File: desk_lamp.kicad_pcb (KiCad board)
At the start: 2 copper layers, 55 x 37 mm, 31 parts, among them J1 CON-SOCJ-2155, J2 CON-SOCJ-2155, J3 Phoenix_Contact_1989764, Q1 2N7002K, Q2 MCB150N06YB-TP, U1 MCP1799T-3302H_DB, U2 MIC5365-1.2YC5-TR, U3 ECS-TXO-25CSMV-320-AM-TR, U4 ICE40LP384-SG32, U5 W25X10CLSNIG

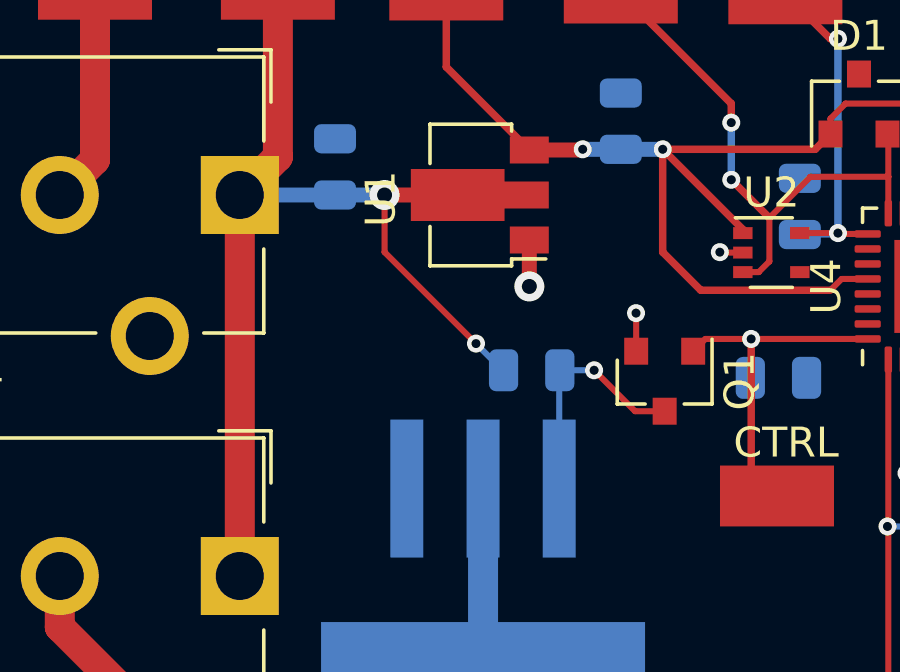
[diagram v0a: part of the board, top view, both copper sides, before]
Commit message: Fixed mosfet swapped pins
Gate and Drain pins were swapped.
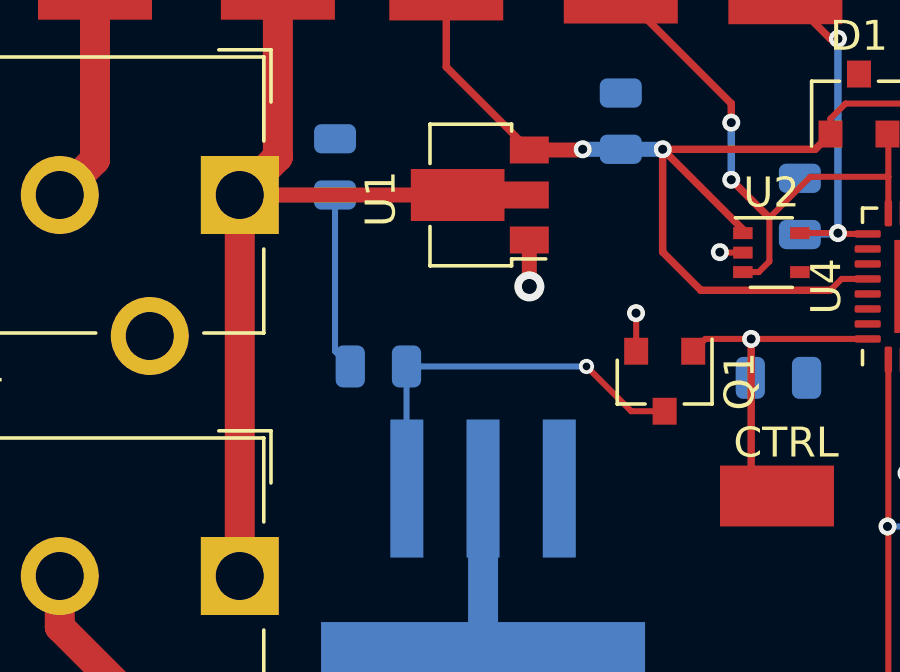
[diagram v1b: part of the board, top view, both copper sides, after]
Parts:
- moved R2 5.11 mm to (68.4, 35.9)
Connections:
- Q2 pad 1: GND -> Net-(Q1-Pad3)
- Q2 pad 3: Net-(Q1-Pad3) -> GND
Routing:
- net Net-(Q1-Pad3): track 8.01 -> 13.3 mm
- net +12V: track 37.1 -> 39.1 mm, vias 2 -> 0
